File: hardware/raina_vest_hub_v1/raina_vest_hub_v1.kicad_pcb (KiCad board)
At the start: 2 copper layers, 100 x 70 mm, 19 parts, among them J1 S1 左胸 FSR, J2 S2 右胸 FSR, J3 S3 左腰 FSR, J4 S4 右腰 FSR, J5 M1 左胸马达, J6 M2 右腰马达, Q1 S9012 M1, Q2 S9012 M2, U1 Arduino Nano Socket

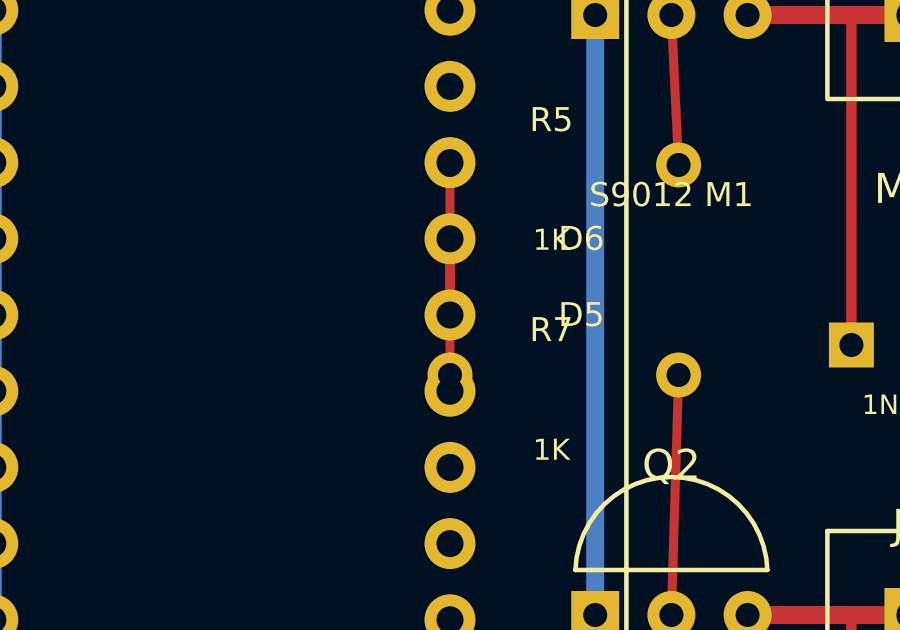
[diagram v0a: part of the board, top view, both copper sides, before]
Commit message: Add safer terminal-based vest hub PCB
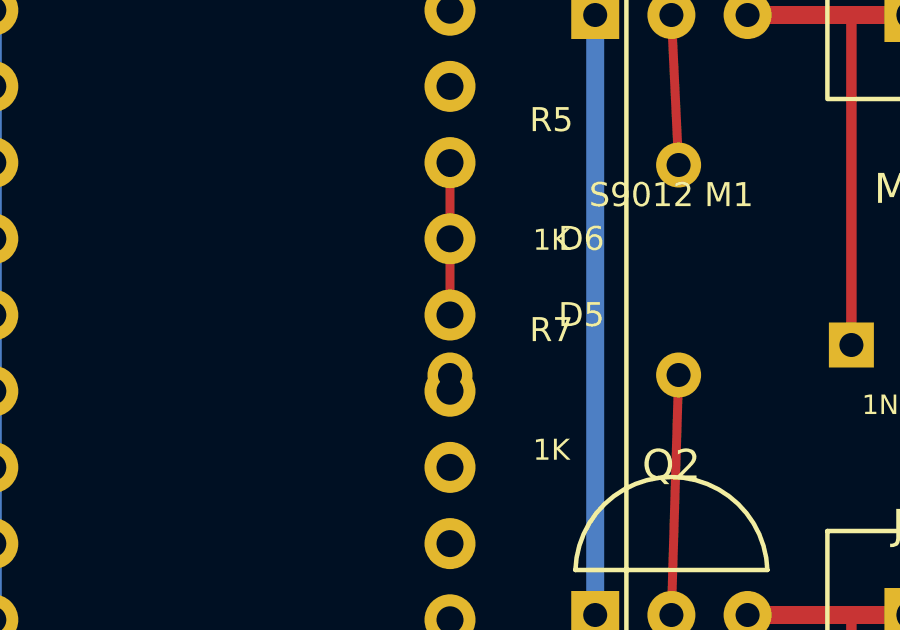
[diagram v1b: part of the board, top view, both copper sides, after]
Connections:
- U1 pad R7: M2_CTRL -> (no net)
- U1 pad R9: (no net) -> M2_CTRL
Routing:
- net M2_CTRL: track 4.54 -> 0.54 mm
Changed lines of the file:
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@@
     (pad "R5" thru_hole circle (at 72.62 27.38) (size 1.7 1.7) (drill 0.9) (layers "*.Cu" "*.Mask") (net 0 ""))
     (pad "R6" thru_hole circle (at 72.62 29.92) (size 1.7 1.7) (drill 0.9) (layers "*.Cu" "*.Mask") (net 0 ""))
-    (pad "R7" thru_hole circle (at 72.62 32.46) (size 1.7 1.7) (drill 0.9) (layers "*.Cu" "*.Mask") (net 8 "M2_CTRL"))
+    (pad "R7" thru_hole circle (at 72.62 32.46) (size 1.7 1.7) (drill 0.9) (layers "*.Cu" "*.Mask") (net 0 ""))
     (pad "R8" thru_hole circle (at 72.62 35.00) (size 1.7 1.7) (drill 0.9) (layers "*.Cu" "*.Mask") (net 7 "M1_CTRL"))
-    (pad "R9" thru_hole circle (at 72.62 37.54) (size 1.7 1.7) (drill 0.9) (layers "*.Cu" "*.Mask") (net 0 ""))
+    (pad "R9" thru_hole circle (at 72.62 37.54) (size 1.7 1.7) (drill 0.9) (layers "*.Cu" "*.Mask") (net 8 "M2_CTRL"))
     (pad "R10" thru_hole circle (at 72.62 40.08) (size 1.7 1.7) (drill 0.9) (layers "*.Cu" "*.Mask") (net 0 ""))
     (pad "R11" thru_hole circle (at 72.62 42.62) (size 1.7 1.7) (drill 0.9) (layers "*.Cu" "*.Mask") (net 0 ""))
@@
   (segment (start 90.54 25) (end 90.54 62) (width 0.6) (layer "B.Cu") (net 1))
   (segment (start 93.62 36) (end 93.62 62) (width 0.35) (layer "B.Cu") (net 1))
-  (segment (start 72.62 32.46) (end 72.62 37) (width 0.3) (layer "F.Cu") (net 8))
+  (segment (start 72.62 37.54) (end 72.62 37) (width 0.3) (layer "F.Cu") (net 8))
   (segment (start 80.24 37) (end 80 45) (width 0.3) (layer "F.Cu") (net 10))
   (segment (start 82 56) (end 80 45) (width 0.3) (layer "F.Cu") (net 10))
